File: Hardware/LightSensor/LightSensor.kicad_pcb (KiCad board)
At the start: 2 copper layers, 23 x 10 mm, 3 parts, among them J1 Conn_01x02, Q1 KPS-3227

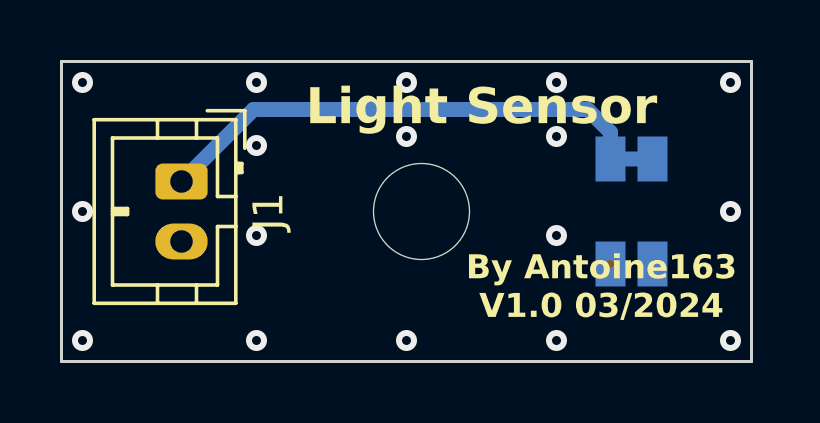
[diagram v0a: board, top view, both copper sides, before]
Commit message: Ajout fichier de production de la carte LightSensor
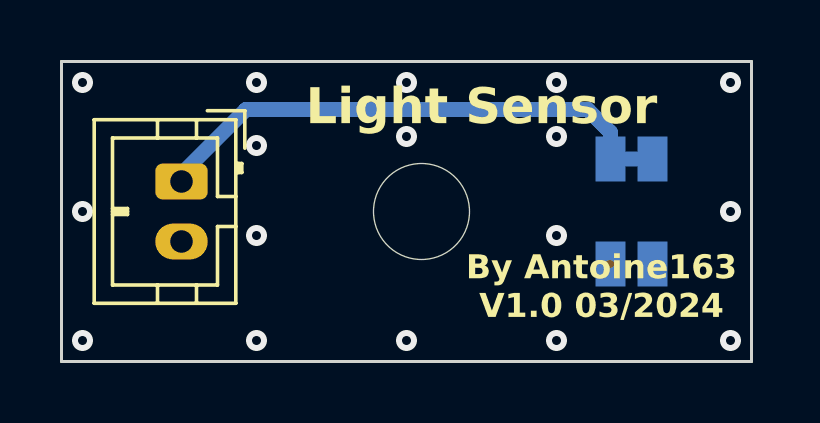
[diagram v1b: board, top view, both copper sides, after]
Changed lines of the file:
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@@
 	(paper "A4")
 	(title_block
-		(title "BleSmartLock - LightSensor")
-		(date "2024-03-16")
+		(title "Ble Smart Lock - Light Sensor")
+		(date "2024-03-31")
 		(rev "1.0")
-		(company "AM163")
-		(comment 4 "AISLER Project ID: BTKFRAHW")
+		(company "antoine163")
 	)
 	(layers
@@
 			(at 1 -2.9 -90)
 			(layer "F.SilkS")
+			(hide yes)
 			(effects
 				(font
@@
 			(at 1 4 -90)
 			(layer "F.Fab")
+			(hide yes)
 			(effects
 				(font
@@
 			)
 		)
+		(property ki_fp_filters "Connector*:*_1x??_*")
+		(sheetname "Root")
+		(sheetfile "LightSensor.kicad_sch")
 		(attr through_hole)
 		(fp_line
@@
 			(at 2.5 1 -90)
 			(layer "B.SilkS")
+			(hide yes)
 			(effects
 				(font
@@
 			(at 0 -3.81 180)
 			(layer "B.Fab")
+			(hide yes)
 			(effects
 				(font
@@
 			)
 		)
+		(property ki_fp_filters "Kingbright*KPS?3227*")
+		(sheetname "Root")
+		(sheetfile "LightSensor.kicad_sch")
 		(attr smd)
 		(fp_line
@@
 		(tags "mounting hole 3.2mm no annular m3")
 		(property "Reference" "H1"
-			(at 0 4.2 270)
+			(at 0 4.2 -90)
 			(layer "B.SilkS")
 			(hide yes)
@@
 			(at 0 -4.2 -90)
 			(layer "B.Fab")
+			(hide yes)
 			(effects
 				(font
@@
 			)
 		)
-		(attr exclude_from_pos_files exclude_from_bom)
+		(property ki_fp_filters "MountingHole*")
+		(sheetname "Root")
+		(sheetfile "LightSensor.kicad_sch")
+		(attr exclude_from_pos_files)
 		(fp_circle
 			(center 0 0)
@@
 		)
 	)
+	(dimension
+		(type aligned)
+		(layer "Cmts.User")
+		(pts
+			(xy 158 84) (xy 135 84)
+		)
+		(height 2.5)
+		(gr_text "23,0000 mm"
+			(at 146.5 80.35 0)
+			(layer "Cmts.User")
+			(effects
+				(font
+					(size 1 1)
+					(thickness 0.15)
+				)
+			)
+		)
+		(format
+			(prefix "")
+			(suffix "")
+			(units 3)
+			(units_format 1)
+			(precision 4)
+		)
+		(style
+			(thickness 0.15)
+			(arrow_length 1.27)
+			(text_position_mode 0)
+			(extension_height 0.58642)
+			(extension_offset 0.5) keep_text_aligned)
+	)
+	(dimension
+		(type aligned)
+		(layer "Cmts.User")
+		(pts
+			(xy 158 94) (xy 158 84)
+		)
+		(height 4.5)
+		(gr_text "10,0000 mm"
+			(at 161.35 89 90)
+			(layer "Cmts.User")
+			(effects
+				(font
+					(size 1 1)
+					(thickness 0.15)
+				)
+			)
+		)
+		(format
+			(prefix "")
+			(suffix "")
+			(units 3)
+			(units_format 1)
+			(precision 4)
+		)
+		(style
+			(thickness 0.15)
+			(arrow_length 1.27)
+			(text_position_mode 0)
+			(extension_height 0.58642)
+			(extension_offset 0.5) keep_text_aligned)
+	)
+	(segment
+		(start 139 87.75)
+		(end 139 88)
+		(width 0.5)
+		(layer "B.Cu")
+		(net 1)
+	)
 	(segment
 		(start 152.54 85.6)
-		(end 141.4 85.6)
+		(end 141.15 85.6)
+		(width 0.5)
+		(layer "B.Cu")
+		(net 1)
+	)
+	(segment
+		(start 153.3 86.36)
+		(end 152.54 85.6)
 		(width 0.5)
 		(layer "B.Cu")
@@
 	)
 	(segment
+		(start 141.15 85.6)
+		(end 139 87.75)
+		(width 0.5)
+		(layer "B.Cu")
+		(net 1)
+	)
+	(segment
 		(start 153.3 87.25)
 		(end 154.7 87.25)
 		(width 0.5)
 		(layer "B.Cu")
-		(net 1)
-	)
-	(segment
-		(start 141.4 85.6)
-		(end 139 88)
-		(width 0.5)
-		(layer "B.Cu")
-		(net 1)
-	)
-	(segment
-		(start 153.3 86.36)
-		(end 152.54 85.6)
-		(width 0.5)
-		(layer "B.Cu")

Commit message: Mise a jour pcb en v1.1 et readme
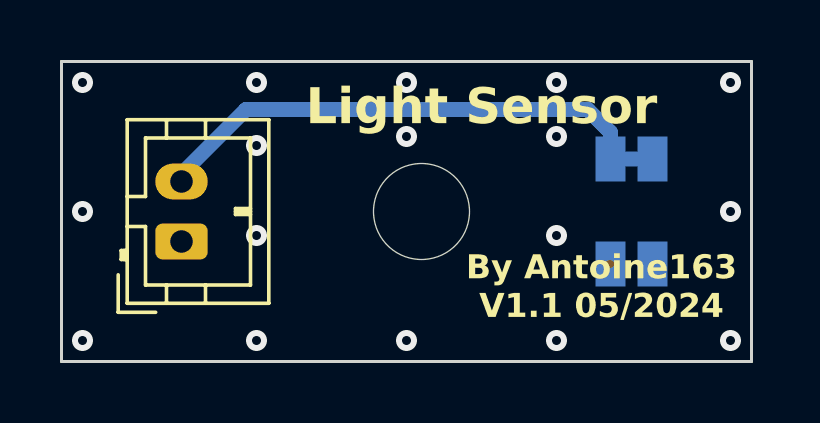
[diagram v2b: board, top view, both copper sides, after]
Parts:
- moved J1 2.00 mm to (139.0, 90.0), turned to 90 degrees
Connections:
- J1 pad 1: Net-(J1-Pin_1) -> GND
- J1 pad 2: GND -> Net-(J1-Pin_2)
- Q1 pad 1: Net-(J1-Pin_1) -> Net-(J1-Pin_2)
- Q1 pad 3: Net-(J1-Pin_1) -> Net-(J1-Pin_2)
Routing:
- net Net-(J1-Pin_2): track 0.00 -> 18.0 mm
- net Net-(J1-Pin_1): track 18.0 -> 0.00 mm
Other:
- board text added: "By Antoine163 V1.1 05/2024"
- board text removed: "By Antoine163 V1.0 03/2024"
